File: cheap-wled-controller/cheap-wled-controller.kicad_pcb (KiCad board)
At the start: 2 copper layers, 14 parts, among them CN1 WJ124-3.81-5P-14-00A, U1 AMS1117-3.3, U2 ESP32-S3-WROOM-1-N4R2, U3 VOLTAGE SELECT, U4 LED DATA LINE LEVEL SHIFTER, U5 CH224K

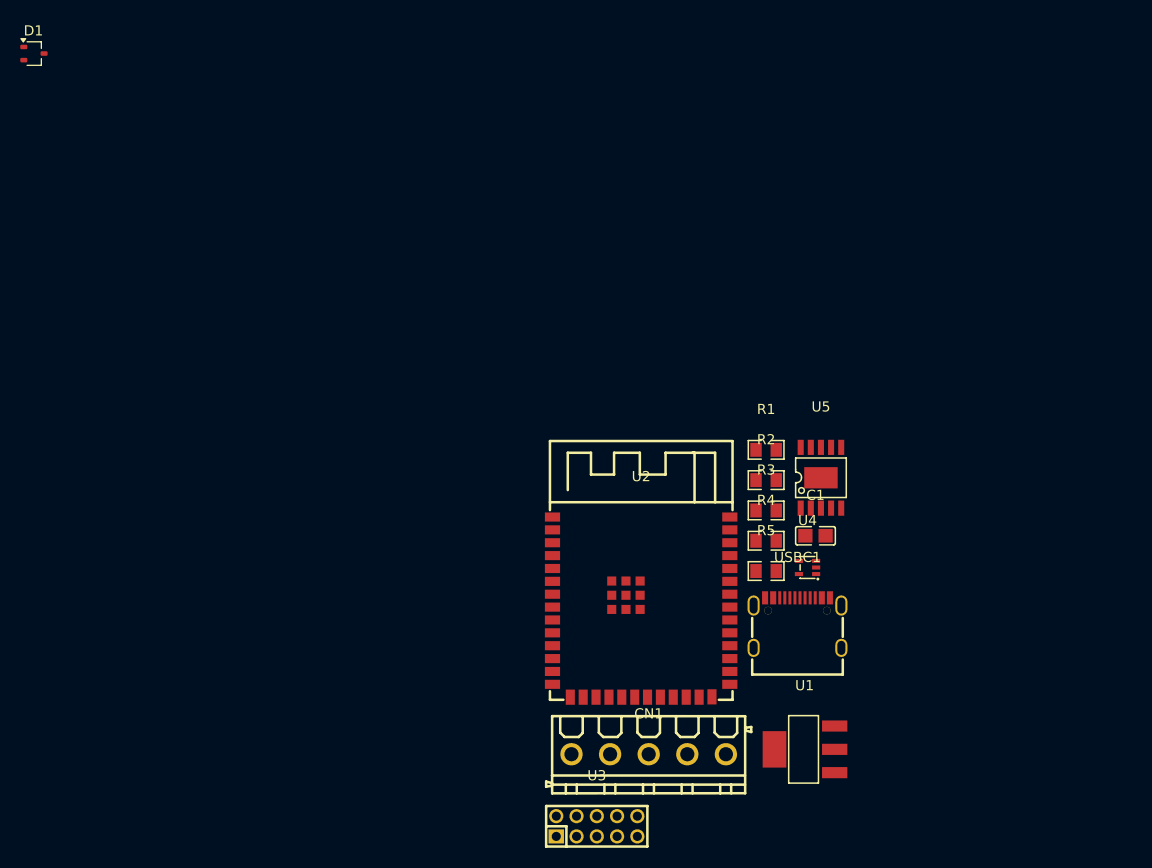
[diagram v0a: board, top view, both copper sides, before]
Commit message: leds added
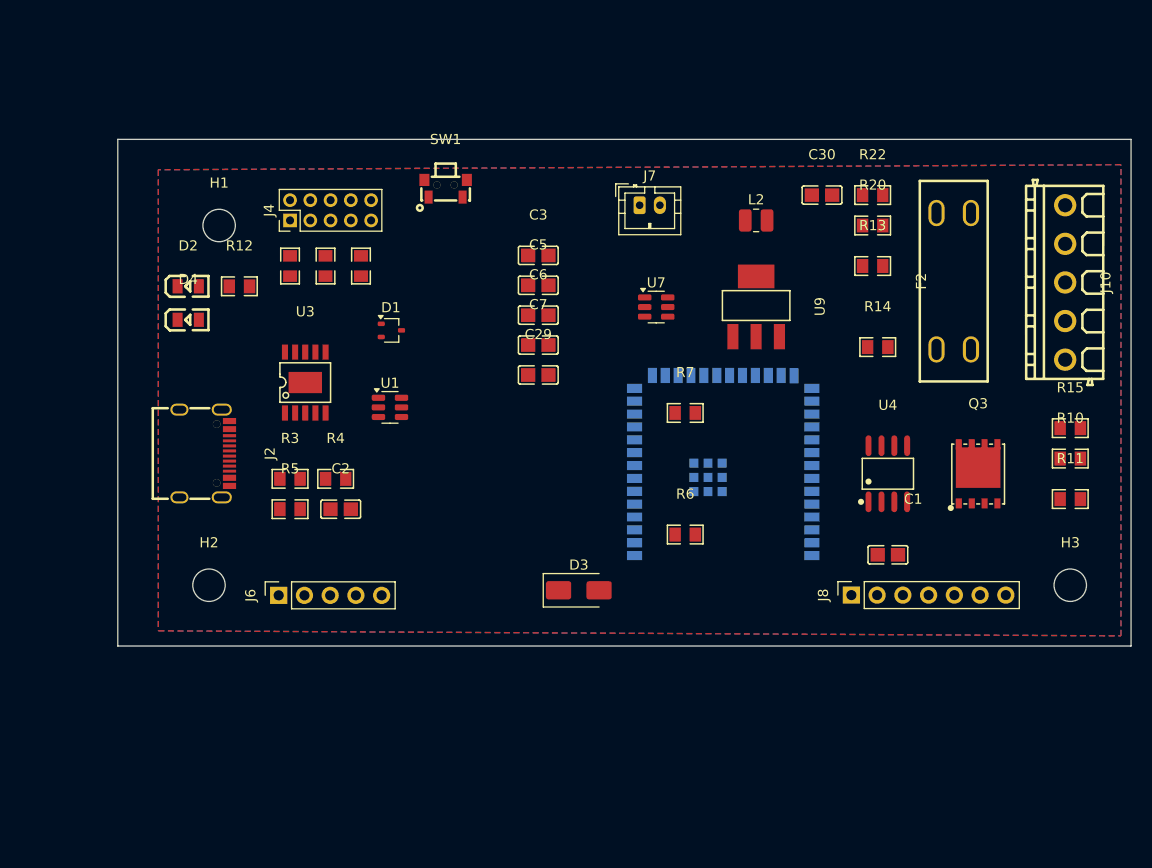
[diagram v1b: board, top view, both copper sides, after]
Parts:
- removed CN1: WJ124-3.81-5P-14-00A, cheap-wled-controller:CONN-TH_5P-P3.81_KF124-3.81-5P
- removed R1: 1k, cheap-wled-controller:R0805
- removed U2: ESP32-S3-WROOM-1-N4R2, cheap-wled-controller:WIRELM-SMD_ESP32-S3-WROOM-1
- removed USBC1: TYPE-C-31-M-12, cheap-wled-controller:USB-C_SMD-TYPE-C-31-M-12
- added C2: 1u, cheap-wled-controller:C0805, F.Cu at (32.0, 46.5)
- added C29: 100n, cheap-wled-controller:C0805, F.Cu at (51.5, 33.2)
- added C3: 0.1u, cheap-wled-controller:C0805, F.Cu at (51.5, 21.4)
- added C30: 56p, cheap-wled-controller:C0805, F.Cu at (79.5, 15.5)
- added C5: 10u, cheap-wled-controller:C0805, F.Cu at (51.5, 24.4)
- added C6: 10u, cheap-wled-controller:C0805, F.Cu at (51.5, 27.4)
- added C7: 10u, cheap-wled-controller:C0805, F.Cu at (51.5, 30.3)
- added D2: LED_Small, cheap-wled-controller:LED0805-R-RD, F.Cu at (16.9, 24.5)
- added D3: ~, Diode_SMD:D_SMA, F.Cu at (55.5, 54.5)
- added D4: LED_Small, cheap-wled-controller:LED0805-R-RD, F.Cu at (16.9, 27.8)
- added F2: DIR, cheap-wled-controller:FUSE-TH_XF-508P-A-B, F.Cu at (92.5, 24.0)
- added H1: ~, MountingHole:MountingHole_3.2mm_M3, F.Cu at (20.0, 18.5)
- added H2: ~, MountingHole:MountingHole_3.2mm_M3, F.Cu at (19.0, 54.0)
- added H3: ~, MountingHole:MountingHole_3.2mm_M3, F.Cu at (104.0, 54.0)
- added J10: Conn_01x05_Pin, cheap-wled-controller:CONN-TH_5P-P3.81_KF124-3.81-5P, F.Cu at (103.5, 24.1)
- added J2: USB_C_Receptacle, cheap-wled-controller:USB-C_SMD-TYPE-C-31-M-12, F.Cu at (18.6, 41.0)
- added J4: Conn_02x05_Odd_Even, Connector_PinHeader_2.00mm:PinHeader_2x05_P2.00mm_Vertical, F.Cu at (27.0, 18.0)
- added J6: Conn_01x05_Pin, Connector_PinSocket_2.54mm:PinSocket_1x05_P2.54mm_Vertical, F.Cu at (25.9, 55.0)
- added J7: Conn_01x02_Pin, Connector_JST:JST_PH_B2B-PH-K_1x02_P2.00mm_Vertical, F.Cu at (61.5, 16.5)
- added J8: Conn_01x07_Pin, Connector_PinSocket_2.54mm:PinSocket_1x07_P2.54mm_Vertical, F.Cu at (82.4, 55.0)
- added L2: 4.7u, Inductor_SMD:L_1008_2520Metric, F.Cu at (73.0, 18.0)
- added Q3: NMOS, cheap-wled-controller:DFN-8_L5.9-W5.2-P1.27-LS6.2-BL, F.Cu at (94.9, 43.0)
- added R10: 10k, cheap-wled-controller:R0805, F.Cu at (104.0, 41.5)
- added R11: 10k, cheap-wled-controller:R0805, F.Cu at (104.0, 45.5)
- added R12: 10k, cheap-wled-controller:R0805, F.Cu at (22.0, 24.5)
- added R13: 27k, cheap-wled-controller:R0805, F.Cu at (84.5, 22.5)
- added R14: 10k, cheap-wled-controller:R0805, F.Cu at (85.0, 30.5)
- added R15: 56k, cheap-wled-controller:R0805, F.Cu at (104.0, 38.5)
- added R16: 24k, cheap-wled-controller:R0805, F.Cu at (30.5, 22.5)
- added R17: 6.8k, cheap-wled-controller:R0805, F.Cu at (27.0, 22.5)
- added R20: 100k, cheap-wled-controller:R0805, F.Cu at (84.5, 18.5)
- added R22: 27k, cheap-wled-controller:R0805, F.Cu at (84.5, 15.5)
- added R6: 4k, cheap-wled-controller:R0805, F.Cu at (66.0, 49.0)
- added R7: 4k, cheap-wled-controller:R0805, F.Cu at (66.0, 37.0)
- added SW1: SW_Push, cheap-wled-controller:SW-SMD_TSA245G00D-250, F.Cu at (42.4, 14.8)
- added U7: TPS54202DDC, Package_TO_SOT_SMD:SOT-23-6, F.Cu at (63.1, 26.6)
- added U9: AMS1117-3.3, cheap-wled-controller:SOT-223-3_L6.5-W3.4-P2.30-LS7.0-BR, F.Cu at (73.0, 26.5)
- C1: value 1u -> 10u
- R2: value 10k -> 56k
- R3: value 6.8k -> 1k
- R4: value 24K -> 10k
- R5: value 56K -> 10k
- U1: value AMS1117-3.3 -> USBLC6-2SC6; footprint cheap-wled-controller:SOT-223-3_L6.5-W3.4-P2.30-LS7.0-BR -> Package_TO_SOT_SMD:SOT-23-6
- U3: value VOLTAGE SELECT -> CH224K; footprint cheap-wled-controller:HDR-TH_10P-P2.00-V-M-R2-C5-S2.00 -> cheap-wled-controller:ESSOP-10_L4.9-W3.9-P1.0-LS6.0-TL-EP
- U4: value LED DATA LINE LEVEL SHIFTER -> MX5014S; footprint cheap-wled-controller:TSSOP-5_L2.0-W1.3-P0.65-LS2.1-BR -> cheap-wled-controller:SOIC-8_L4.9-W3.9-P1.27-LS6.0-BL
- U5: value CH224K -> ESP32-S3-WROOM-1-N4R2; footprint cheap-wled-controller:ESSOP-10_L4.9-W3.9-P1.0-LS6.0-TL-EP -> cheap-wled-controller:WIRELM-SMD_ESP32-S3-WROOM-1; moved to B.Cu
- moved U1 53.0 mm to (36.9, 36.5)
- moved U3 52.4 mm to (28.5, 34.0)
- moved R5 47.4 mm to (27.0, 46.5)
- moved R3 47.1 mm to (27.0, 43.5)
- moved R2 45.2 mm to (34.0, 22.5), turned to 90 degrees
- moved D1 44.6 mm to (37.0, 28.9)
- moved R4 42.9 mm to (31.5, 43.5)
- moved U4 12.2 mm to (86.0, 43.0)
- moved U5 9.72 mm to (69.8, 42.2)
- moved C1 7.39 mm to (86.0, 51.0)
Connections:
- C1 pad 1: /VDD_C -> GND
- C1 pad 2: /GND -> /V_LED
- D1 pad 3: /GND -> GND
- R2 pad 1: Net-(U5-VBUS) -> GND
- R3 pad 1: /GND -> /VDD_C
- R3 pad 2: Net-(R3-Pad2) -> /VBUS_C
- R4 pad 1: unconnected-(R4-Pad1) -> Net-(U3-VBUS)
- R4 pad 2: Net-(R4-Pad2) -> /VBUS_C
- R5 pad 1: unconnected-(R5-Pad1) -> Net-(U3-PG)
- R5 pad 2: Net-(R5-Pad2) -> /VDD_C
- U1 pad 1: /GND -> /D-
- U1 pad 2: unconnected-(U1-VOUT-Pad2) -> GND
- U1 pad 3: /5v -> /D+
- U1 pad 4: /3.3v -> /D+_OUT
- U3 pad 1: unconnected-(U3-Pad1) -> /VDD_C
- U3 pad 10: /VDD_C -> Net-(U3-PG)
- U3 pad 3: Net-(U5-CFG1) -> unconnected-(U3-CFG3-Pad3)
- U3 pad 4: Net-(R5-Pad2) -> unconnected-(U3-DP-Pad4)
- U3 pad 5: Net-(U5-CFG1) -> unconnected-(U3-DM-Pad5)
- U3 pad 6: Net-(R4-Pad2) -> Net-(D1-K1)
- U3 pad 7: Net-(U5-CFG1) -> Net-(D1-K2)
- U3 pad 8: Net-(R3-Pad2) -> Net-(U3-VBUS)
- U3 pad 9: Net-(U5-CFG1) -> Net-(J4-Pin_10)
- U4 pad 1: unconnected-(U4-NC-Pad1) -> /V_LED
- U4 pad 2: /LED_DATA -> /MOS_1
- U4 pad 3: /GND -> /LED_1_VCC
- U4 pad 4: /DATA_OUTPUT -> GND
- U4 pad 5: /5v -> Net-(Q3-G)
- U5 pad 1: /VDD_C -> unconnected-(U5-GND-Pad1)
- U5 pad 11: /GND -> /GPIO18
- U5 pad 2: unconnected-(U5-CFG2-Pad2) -> +3.3V
- U5 pad 3: unconnected-(U5-CFG3-Pad3) -> Net-(U5-EN)
- U5 pad 4: unconnected-(U5-DP-Pad4) -> /GPIO4
- U5 pad 5: unconnected-(U5-DM-Pad5) -> /GPIO5
- U5 pad 6: Net-(D1-K2) -> /GPIO6
- U5 pad 7: Net-(D1-K1) -> /VOLT_OUT
- U5 pad 8: Net-(U5-VBUS) -> unconnected-(U5-IO15-Pad8)
- U5 pad 9: Net-(U5-CFG1) -> unconnected-(U5-IO16-Pad9)
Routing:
- added copper zone on B.Cu, net GND
- added copper zone on F.Cu, net GND
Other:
- board outline added: 100 x 50 mm

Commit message: some traces
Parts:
- moved J2 2.50 mm to (17.1, 39.0)
- moved J10 1.99 mm to (105.0, 22.8)
- moved SW1 1.64 mm to (43.6, 13.8)
- moved U5 0.92 mm to (69.8, 43.1)
- moved R4 0.50 mm to (32.0, 43.5)
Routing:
- net GND: track 0.00 -> 168.9 mm, vias 0 -> 3
- net +3.3V: track 0.00 -> 98.2 mm
- net /VBUS_C: track 0.00 -> 92.8 mm, vias 0 -> 4
- net /V_LED: track 0.00 -> 62.6 mm, vias 0 -> 2
- net /GPIO5: track 0.00 -> 42.9 mm, vias 0 -> 2
- net /GPIO4: track 0.00 -> 38.7 mm, vias 0 -> 2
- net +5V: track 0.00 -> 35.4 mm, vias 0 -> 2
- net /D-: track 0.00 -> 34.1 mm, vias 0 -> 2
- net /MOS_1: track 0.00 -> 28.2 mm, vias 0 -> 1
- net Net-(U5-EN): track 0.00 -> 26.7 mm, vias 0 -> 1
- net /FB: track 0.00 -> 21.0 mm
- net Net-(D1-K2): track 0.00 -> 17.6 mm
- net Net-(D1-K1): track 0.00 -> 17.5 mm
- net /D+: track 0.00 -> 16.8 mm, vias 0 -> 2
- net Net-(D4-A): track 0.00 -> 7.35 mm
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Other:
- board size 100 x 50 mm -> 98 x 48 mm

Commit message: pcb fixes
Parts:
- U5: moved to F.Cu
- moved R6 15.7 mm to (51.5, 43.0)
- moved R7 14.8 mm to (51.5, 40.0)
- moved D3 4.00 mm to (51.5, 54.5)
- moved R10 1.58 mm to (105.5, 41.0)
- moved R11 1.58 mm to (105.5, 45.0)
- moved R15 1.58 mm to (105.5, 38.0)
- moved C1 1.41 mm to (85.0, 50.0)
- moved U4 1.41 mm to (85.0, 42.0)
- moved J7 1.12 mm to (61.0, 15.5)
- moved J2 1.00 mm to (16.1, 39.0)
- moved D2 0.78 mm to (16.6, 23.8)
- moved J6 0.70 mm to (25.9, 54.3)
- moved D4 0.55 mm to (16.4, 27.8)
- moved Q3 0.51 mm to (95.0, 42.5)
- moved R14 0.50 mm to (84.5, 30.5)
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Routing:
- net GND: track 168.9 -> 5.62 mm, vias 3 -> 5
- net Net-(D2-A): track 0.00 -> 82.1 mm, vias 0 -> 2
- net /LED_DATA: track 0.00 -> 66.7 mm, vias 0 -> 2
- net /GPIO6: track 0.00 -> 62.3 mm, vias 0 -> 2
- net /GPIO36: track 0.00 -> 48.4 mm, vias 0 -> 2
- net /VBUS_C: track 92.8 -> 141.1 mm
- net /LED_1_VCC: track 3.81 -> 51.8 mm, vias 0 -> 2
- net /GPIO37: track 0.00 -> 46.9 mm, vias 0 -> 2
- net /D-_OUT: track 0.00 -> 46.6 mm
- net /VDD_C: track 0.00 -> 46.0 mm, vias 0 -> 2
- net /D+_OUT: track 0.00 -> 43.9 mm
- net Net-(U5-IO0): track 0.00 -> 42.0 mm, vias 0 -> 2
- net /GPIO38: track 0.00 -> 41.1 mm, vias 0 -> 2
- net /RX: track 0.00 -> 34.0 mm, vias 0 -> 1
- net /SW_5V: track 0.00 -> 33.2 mm, vias 0 -> 2
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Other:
- outline, holes or cut-outs redrawn

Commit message: drc fixes
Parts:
- removed Q3: NMOS, cheap-wled-controller:DFN-8_L5.9-W5.2-P1.27-LS6.2-BL
- added REF**: DFN-8_L5.9-W5.2-P1.27-LS6.2-BL, cheap-wled-controller:DFN-8_L5.9-W5.2-P1.27-LS6.2-BL, F.Cu at (95.0, 42.5)
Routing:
- net Net-(Q3-G): track 15.6 -> 24.6 mm
- net /LED_1_VCC: track 51.8 -> 54.8 mm
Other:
- outline, holes or cut-outs redrawn

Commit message: drc fixes
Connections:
- J2 pad 0: (no net) -> Earth
- J2 pad 1: (no net) -> Earth
- J2 pad 2: (no net) -> Earth
- J2 pad 3: (no net) -> Earth
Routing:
- net +3.3V: track 130.2 -> 135.9 mm
- net /VBUS_C: track 141.1 -> 143.4 mm
- net Net-(D2-A): track 82.1 -> 84.1 mm
- net /BOOT: track 20.5 -> 21.6 mm
- net /VOLT_OUT: track 34.7 -> 35.3 mm

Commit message: drc fixes
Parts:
- moved SW1 0.50 mm to (43.6, 14.3)
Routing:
- net GND: track 5.62 -> 19.8 mm, vias 5 -> 7
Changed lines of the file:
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@@
 	(footprint "cheap-wled-controller:SW-SMD_TSA245G00D-250"
 		(layer "F.Cu")
-		(at 43.65 13.85)
+		(at 43.65 14.35)
 		(property "Reference" "SW1"
 			(at 0 -4.85 0)
@@
 	)
 	(via
+		(at 83.2739 48.021843)
+		(size 0.6)
+		(drill 0.3)
+		(layers "F.Cu" "B.Cu")
+		(free yes)
+		(net 8)
+	)
+	(via
+		(at 86.5 43)
+		(size 0.6)
+		(drill 0.3)
+		(layers "F.Cu" "B.Cu")
+		(net 8)
+	)
+	(via
 		(at 20.9 35.5)
 		(size 0.6)
@@
 	)
 	(segment
+		(start 83.2739 46.2261)
+		(end 86.5 43)
+		(width 0.2)
+		(layer "B.Cu")
+		(net 8)
+	)
+	(segment
+		(start 84.021843 48.021843)
+		(end 89 53)
+		(width 0.2)
+		(layer "B.Cu")
+		(net 8)
+	)
+	(segment
+		(start 83.2739 48.021843)
+		(end 84.021843 48.021843)
+		(width 0.2)
+		(layer "B.Cu")
+		(net 8)
+	)
+	(segment
+		(start 83.2739 48.021843)
+		(end 83.2739 46.2261)
+		(width 0.2)
+		(layer "B.Cu")
+		(net 8)
+	)
+	(segment
 		(start 82.1425 53.7733)
 		(end 82.4 53.7733)
@@
 	)
 	(segment
+		(start 64.9646 18)
+		(end 71.925 18)
+		(width 0.2)
+		(layer "F.Cu")
+		(net 13)
+	)
+	(segment
 		(start 54.472 32.2733)
 		(end 50.5 32.2733)
@@
 	)
 	(segment
-		(start 71.925 18)
-		(end 64.9646 18)
-		(width 0.2)
-		(layer "F.Cu")
-		(net 13)
-	)
-	(segment
 		(start 60.3995 27.5194)
 		(end 59.2259 27.5194)
@@
 	)
 	(segment
-		(start 64.9646 18)
-		(end 63.9765 18.9881)
+		(start 62 26.55)
+		(end 61.3689 26.55)
 		(width 0.2)
 		(layer "F.Cu")
@@
 	)
 	(segment
-		(start 62 26.55)
-		(end 61.3689 26.55)
+		(start 64.7323 18.2323)
+		(end 64.9646 18)
 		(width 0.2)
 		(layer "F.Cu")
@@
 	)
 	(via
-		(at 63.9765 18.9881)
+		(at 64.7323 18.2323)
 		(size 0.6)
 		(drill 0.3)
@@
 	)
 	(segment
-		(start 60.3995 22.5651)
-		(end 60.3995 27.5194)
+		(start 64.7323 18.2323)
+		(end 60.3995 22.5651)
 		(width 0.2)
 		(layer "B.Cu")
@@
 	)
 	(segment
-		(start 63.9765 18.9881)
-		(end 60.3995 22.5651)
+		(start 60.3995 22.5651)
+		(end 60.3995 27.5194)
 		(width 0.2)
 		(layer "B.Cu")
@@
 	)
 	(segment
+		(start 31.901683 58.6273)
+		(end 56.7677 58.6273)
+		(width 0.2)
+		(layer "F.Cu")
+		(net 26)
+	)
+	(segment
 		(start 65.8252 48.0655)
 		(end 65.5982 47.8385)
@@
 	)
 	(segment
-		(start 65.5982 47.8385)
-		(end 62.8467 47.8385)
+		(start 31.664085 58.389702)
+		(end 31.901683 58.6273)
 		(width 0.2)
 		(layer "F.Cu")
@@
 	)
 	(segment
-		(start 56.7677 58.6273)
-		(end 31.2427 58.6273)
+		(start 65.5982 47.8385)
+		(end 62.8467 47.8385)
 		(width 0.2)
 		(layer "F.Cu")
@@
 	)
 	(segment
-		(start 62.8467 47.8385)
-		(end 62.6733 48.0119)
+		(start 56.7677 58.6273)
+		(end 58.4335 56.9615)
 		(width 0.2)
 		(layer "F.Cu")
@@
 	)
 	(segment
-		(start 58.4335 56.9615)
-		(end 56.7677 58.6273)
+		(start 62.8467 47.8385)
+		(end 62.6733 48.0119)
 		(width 0.2)
 		(layer "F.Cu")
@@
 	)
 	(via
-		(at 31.2427 58.6273)
+		(at 31.664085 58.389702)
 		(size 0.6)
 		(drill 0.3)
@@
 	)
 	(segment
-		(start 30.96 58.3446)
-		(end 30.96 55)
+		(start 57.8491 56.3771)
+		(end 58.4335 56.9615)
 		(width 0.2)
 		(layer "B.Cu")
@@
 	)
 	(segment
-		(start 31.2427 58.6273)
-		(end 30.96 58.3446)
+		(start 57.8491 52.8361)
+		(end 57.8491 56.3771)
 		(width 0.2)
 		(layer "B.Cu")
@@
 	)
 	(segment
-		(start 57.8491 56.3771)
-		(end 58.4335 56.9615)
+		(start 30.96 57.685617)
+		(end 30.96 55)
 		(width 0.2)
 		(layer "B.Cu")
@@
 	)
 	(segment
-		(start 57.8491 52.8361)
-		(end 57.8491 56.3771)
+		(start 62.6733 48.0119)
+		(end 57.8491 52.8361)
 		(width 0.2)
 		(layer "B.Cu")
@@
 	)
 	(segment
-		(start 62.6733 48.0119)
-		(end 57.8491 52.8361)
+		(start 31.664085 58.389702)
+		(end 30.96 57.685617)
 		(width 0.2)
 		(layer "B.Cu")
@@
 	)
 	(segment
-		(start 89.007 49.5)
-		(end 94.394 49.5)
-		(width 0.8)
-		(layer "B.Cu")
-		(net 34)
-	)
-	(segment
-		(start 86.3475 46.8405)
-		(end 89.007 49.5)
-		(width 0.8)
-		(layer "B.Cu")
-		(net 34)
-	)
-	(segment
-		(start 99.3163 47.1837)
-		(end 96.7103 47.1837)
-		(width 0.8)
-		(layer "B.Cu")
-		(net 34)
-	)
-	(segment
 		(start 96.7103 27.2897)
 		(end 96.7103 38)
@@
 	)
 	(segment
-		(start 100 41.2897)
-		(end 100 46.5)
+		(start 97.5 49.5)
+		(end 100 47)
 		(width 0.8)
 		(layer "B.Cu")
@@
 	)
 	(segment
-		(start 105 19)
-		(end 105 15.19)
+		(start 100 47)
+		(end 100 41.2897)
 		(width 0.8)
 		(layer "B.Cu")
@@
 	)
 	(segment
-		(start 96.7103 47.1837)
-		(end 96.7103 47.3411)
+		(start 105 19)
+		(end 105 15.19)
 		(width 0.8)
 		(layer "B.Cu")
@@
 	)
 	(segment
-		(start 100 46.5)
-		(end 99.3163 47.1837)
+		(start 86.3475 46.8405)
+		(end 89.007 49.5)
 		(width 0.8)
 		(layer "B.Cu")
@@
 	)
 	(segment
-		(start 96.7103 38)
-		(end 100 41.2897)
+		(start 100 41.2897)
+		(end 96.7103 38)
 		(width 0.8)
 		(layer "B.Cu")
@@
 	)
 	(segment
-		(start 94.394 49.5)
-		(end 96.7103 47.1837)
+		(start 105 19)
+		(end 96.7103 27.2897)
 		(width 0.8)
 		(layer "B.Cu")
@@
 	)
 	(segment
-		(start 105 19)
-		(end 96.7103 27.2897)
+		(start 89.007 49.5)
+		(end 97.5 49.5)
 		(width 0.8)
 		(layer "B.Cu")
